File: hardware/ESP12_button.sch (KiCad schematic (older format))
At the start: 7 parts

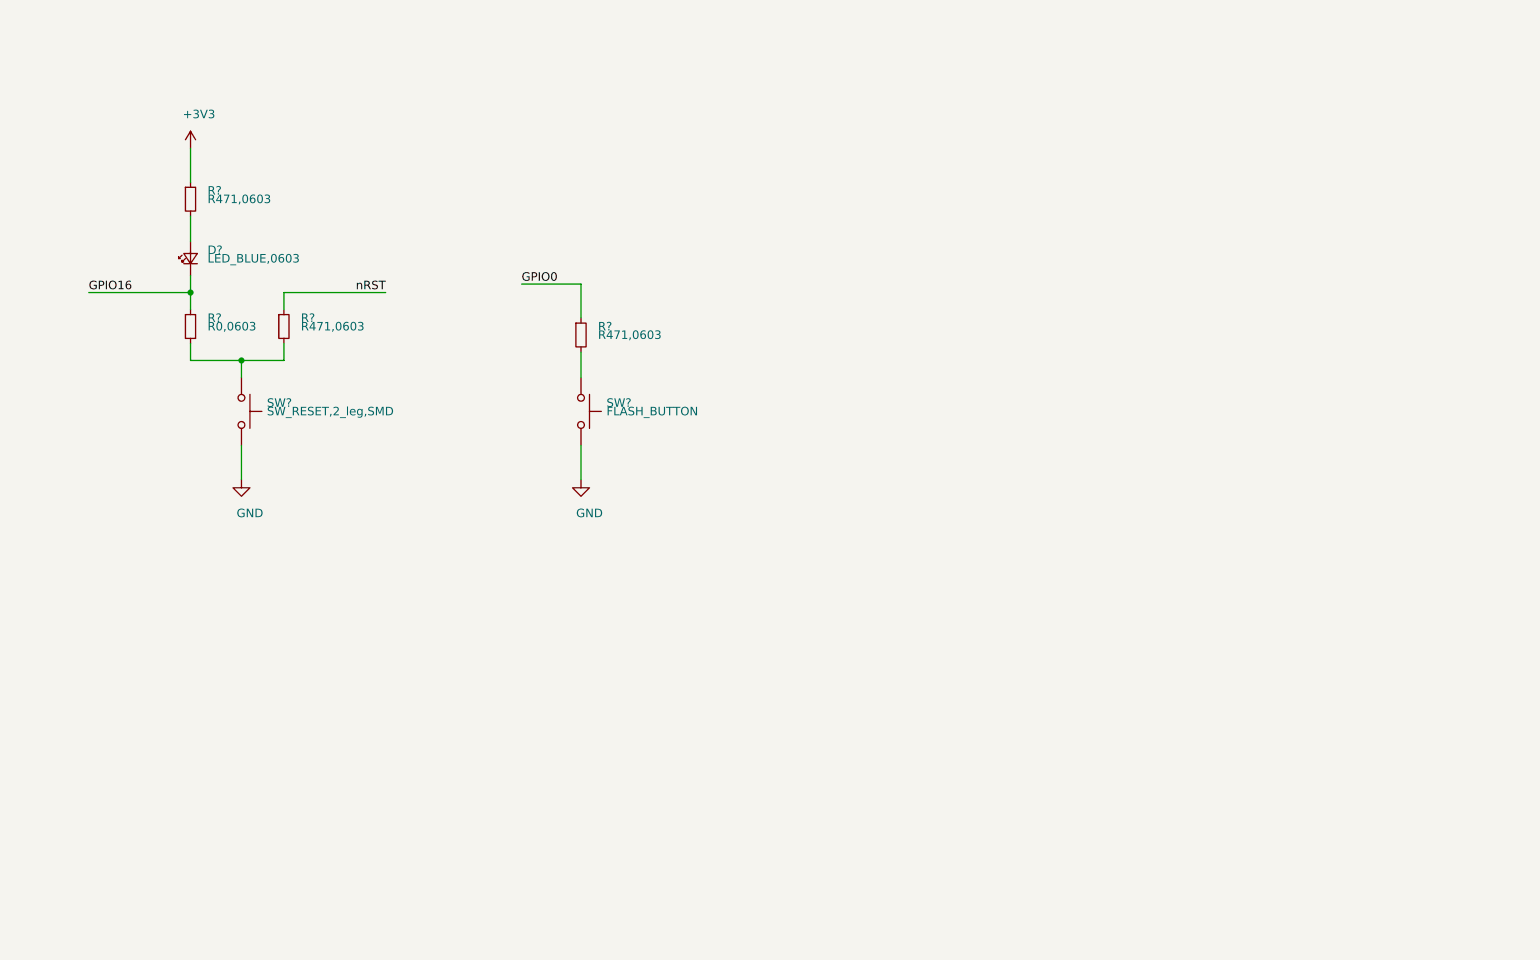
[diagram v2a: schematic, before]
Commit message: update WS2812\,
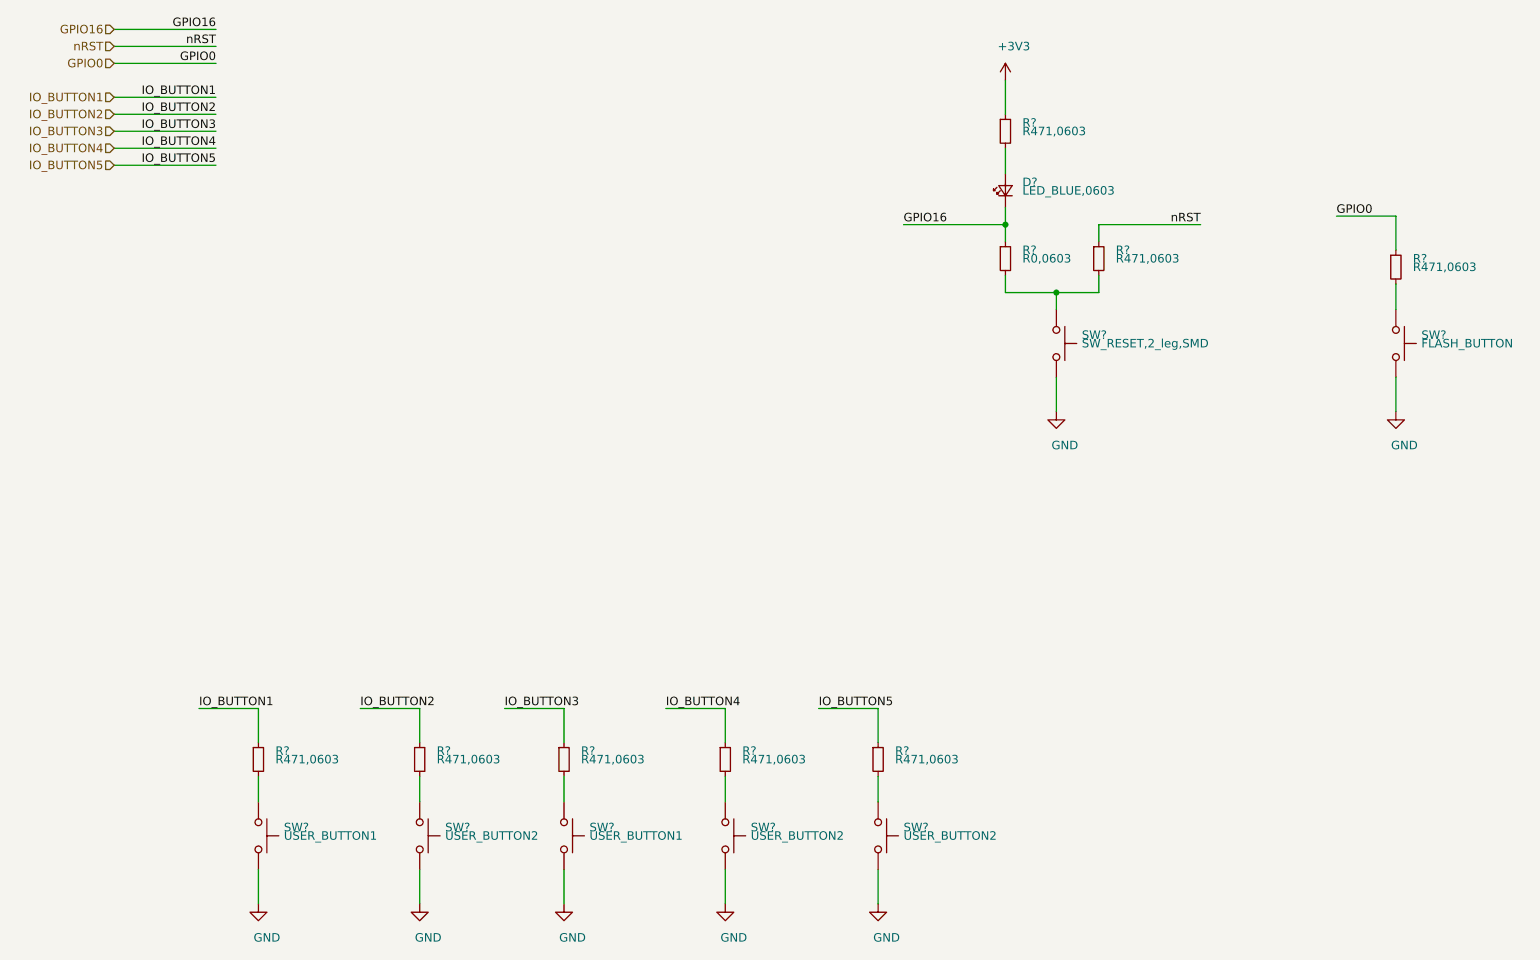
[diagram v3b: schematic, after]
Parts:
- added R? (x5): R471,0603, Resistor_SMD:R_0603_1608Metric_Pad1.05x0.95mm_HandSolder, symbol taobao-r:R471,0603
- added SW? (x2): USER_BUTTON1, footprint-lib:SW_SPST_CK_RS282G05A3, symbol taobao-button:SW_RESET,2_leg,SMD
- added SW? (x3): USER_BUTTON2, footprint-lib:SW_SPST_CK_RS282G05A3, symbol taobao-button:SW_RESET,2_leg,SMD
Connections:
- net GND: now also SW?.2, SW?.2, SW?.2, SW?.2, SW?.2
- new net: R?.2, SW?.1 (x5)
- new net IO_BUTTON1: R?.1
- new net IO_BUTTON2: R?.1
- new net IO_BUTTON3: R?.1
- new net IO_BUTTON4: R?.1
- new net IO_BUTTON5: R?.1
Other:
- moved on the sheet: D?, R?, SW?
